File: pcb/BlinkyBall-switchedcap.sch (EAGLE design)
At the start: 21 parts, among them U1 Tiny85-20-SMT

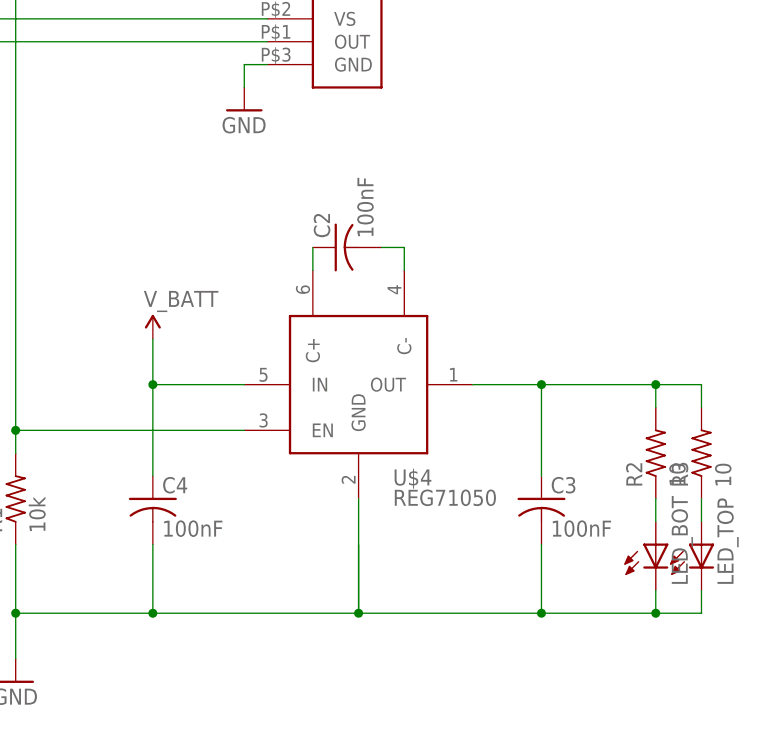
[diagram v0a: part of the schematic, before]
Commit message: RevC pcb design: rounded rect, switch IR pinout, space out test points
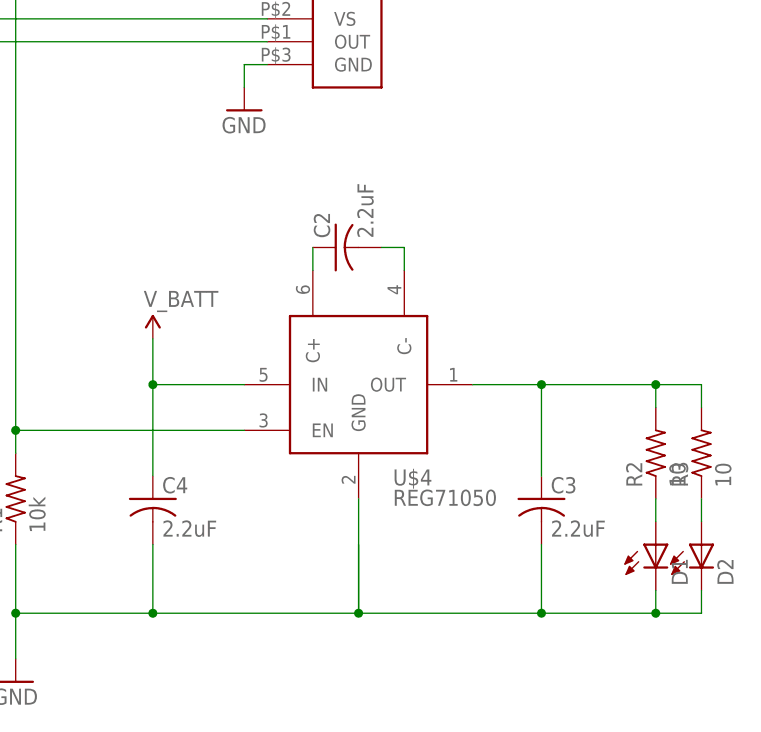
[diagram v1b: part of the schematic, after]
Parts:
- C2, C3, C4: value 100nF -> 2.2uF
- renumbered LED_BOT to D1, LED_TOP to D2, U$2 to U$1
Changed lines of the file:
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@@
 <parts>
 <part name="U1" library="SparkFun-DigitalIC" deviceset="ATTINY45" device="TINY85-20-SMT" value="Tiny85-20-SMT"/>
-<part name="U$2" library="blinkinlabs" deviceset="BATTERY_BUTTON_CELL" device="AG3" value="BATTERY_BUTTON_CELLAG3"/>
+<part name="U$1" library="blinkinlabs" deviceset="BATTERY_BUTTON_CELL" device="AG3" value="BATTERY_BUTTON_CELLAG3"/>
 <part name="SUPPLY1" library="SparkFun-Aesthetics" deviceset="V_BATT" device=""/>
 <part name="GND1" library="SparkFun-Aesthetics" deviceset="GND" device=""/>
@@
 <part name="TP5" library="SparkFun-Passives" deviceset="TEST-POINT" device="3X5"/>
 <part name="TP6" library="SparkFun-Passives" deviceset="TEST-POINT" device="3X5"/>
-<part name="LED_BOT" library="adafruit" deviceset="LED" device="5MM"/>
-<part name="LED_TOP" library="adafruit" deviceset="LED" device="5MM"/>
+<part name="D1" library="adafruit" deviceset="LED" device="5MM"/>
+<part name="D2" library="adafruit" deviceset="LED" device="5MM"/>
 <part name="GND5" library="SparkFun-Aesthetics" deviceset="GND" device=""/>
 <part name="SUPPLY5" library="SparkFun-Aesthetics" deviceset="V_BATT" device=""/>
@@
 <part name="U$3" library="blinkinlabs" deviceset="SW-18015P" device=""/>
 <part name="U$4" library="blinkinlabs" deviceset="REG71050" device=""/>
-<part name="C2" library="adafruit" deviceset="C-US" device="C0603" value="100nF"/>
-<part name="C3" library="adafruit" deviceset="C-US" device="C0603" value="100nF"/>
-<part name="C4" library="adafruit" deviceset="C-US" device="C0603" value="100nF"/>
+<part name="C2" library="adafruit" deviceset="C-US" device="C0603" value="2.2uF"/>
+<part name="C3" library="adafruit" deviceset="C-US" device="C0603" value="2.2uF"/>
+<part name="C4" library="adafruit" deviceset="C-US" device="C0603" value="2.2uF"/>
 </parts>
 <sheets>
@@
 <instances>
 <instance part="U1" gate="G$1" x="30.48" y="68.58"/>
-<instance part="U$2" gate="G$1" x="-33.02" y="68.58"/>
+<instance part="U$1" gate="G$1" x="-33.02" y="68.58"/>
 <instance part="SUPPLY1" gate="G$1" x="-33.02" y="83.82"/>
 <instance part="GND1" gate="1" x="-33.02" y="53.34"/>
@@
 <instance part="TP5" gate="G$1" x="2.54" y="63.5" rot="R180"/>
 <instance part="TP6" gate="G$1" x="45.72" y="83.82" rot="R90"/>
-<instance part="LED_BOT" gate="G$1" x="154.94" y="10.16"/>
-<instance part="LED_TOP" gate="G$1" x="160.02" y="10.16"/>
+<instance part="D1" gate="G$1" x="154.94" y="10.16"/>
+<instance part="D2" gate="G$1" x="160.02" y="10.16"/>
 <instance part="GND5" gate="1" x="83.82" y="-5.08"/>
 <instance part="SUPPLY5" gate="G$1" x="99.06" y="33.02"/>
@@
 <segment>
 <pinref part="SUPPLY1" gate="G$1" pin="V_BATT"/>
-<pinref part="U$2" gate="G$1" pin="+"/>
+<pinref part="U$1" gate="G$1" pin="+"/>
 <wire x1="-33.02" y1="83.82" x2="-33.02" y2="78.74" width="0.1524" layer="91"/>
 </segment>
@@
 <net name="GND" class="0">
 <segment>
-<pinref part="U$2" gate="G$1" pin="-"/>
+<pinref part="U$1" gate="G$1" pin="-"/>
 <wire x1="-33.02" y1="60.96" x2="-33.02" y2="55.88" width="0.1524" layer="91"/>
 <pinref part="GND1" gate="1" pin="GND"/>
@@
 <junction x="99.06" y="2.54"/>
 <junction x="83.82" y="2.54"/>
-<pinref part="LED_BOT" gate="G$1" pin="C"/>
+<pinref part="D1" gate="G$1" pin="C"/>
 <wire x1="154.94" y1="5.08" x2="154.94" y2="2.54" width="0.1524" layer="91"/>
 <wire x1="154.94" y1="2.54" x2="160.02" y2="2.54" width="0.1524" layer="91"/>
-<pinref part="LED_TOP" gate="G$1" pin="C"/>
+<pinref part="D2" gate="G$1" pin="C"/>
 <wire x1="160.02" y1="2.54" x2="160.02" y2="5.08" width="0.1524" layer="91"/>
 <junction x="154.94" y="2.54"/>
@@
 <segment>
 <pinref part="R3" gate="G$1" pin="1"/>
-<pinref part="LED_TOP" gate="G$1" pin="A"/>
+<pinref part="D2" gate="G$1" pin="A"/>
 <wire x1="160.02" y1="15.24" x2="160.02" y2="12.7" width="0.1524" layer="91"/>
 </segment>
@@
 <segment>
 <pinref part="R2" gate="G$1" pin="1"/>
-<pinref part="LED_BOT" gate="G$1" pin="A"/>
+<pinref part="D1" gate="G$1" pin="A"/>
 <wire x1="154.94" y1="15.24" x2="154.94" y2="12.7" width="0.1524" layer="91"/>
 </segment>
